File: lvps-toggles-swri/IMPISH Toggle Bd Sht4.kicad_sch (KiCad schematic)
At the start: 66 parts, among them J5 BCS-110-L-D-TE, J6 BCS-110-L-D-TE, Q13 MMBT3904Q, Q14 MMBT3906Q, Q15 ZXM61N02F, Q16 MMBT3904Q, Q17 MMBT3906Q, Q18 ZXM61N02F, Q19 MMBT3904Q, Q20 MMBT3906Q, Q21 ZXM61N02F, Q22 MMBT3904Q, Q23 MMBT3906Q, Q24 ZXM61N02F, U10 BSP452, U11 AP22804AW5-7, U12 AP22804AW5-7, U7 BSP452, U8 AP22804AW5-7, U9 AP22804AW5-7

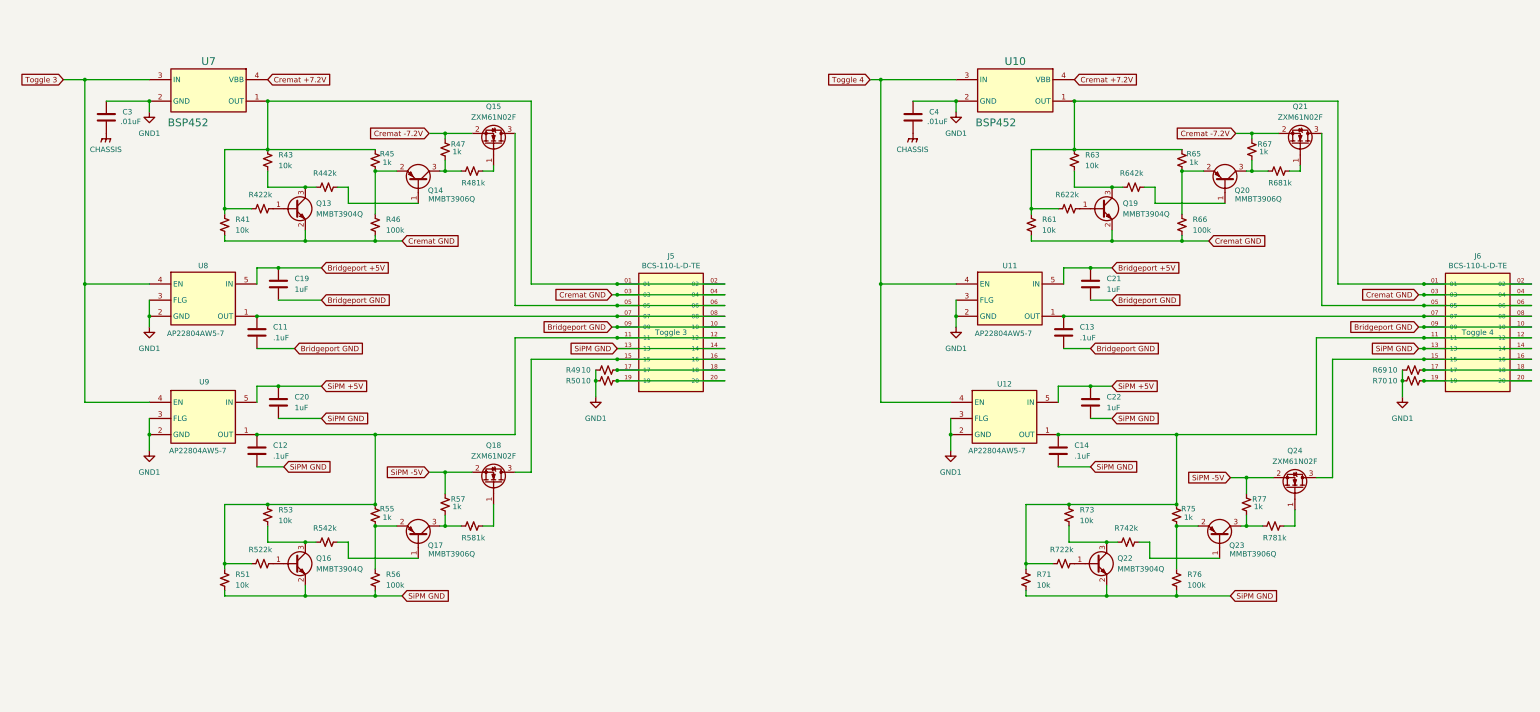
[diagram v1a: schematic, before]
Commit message: swri toggles: start one ground
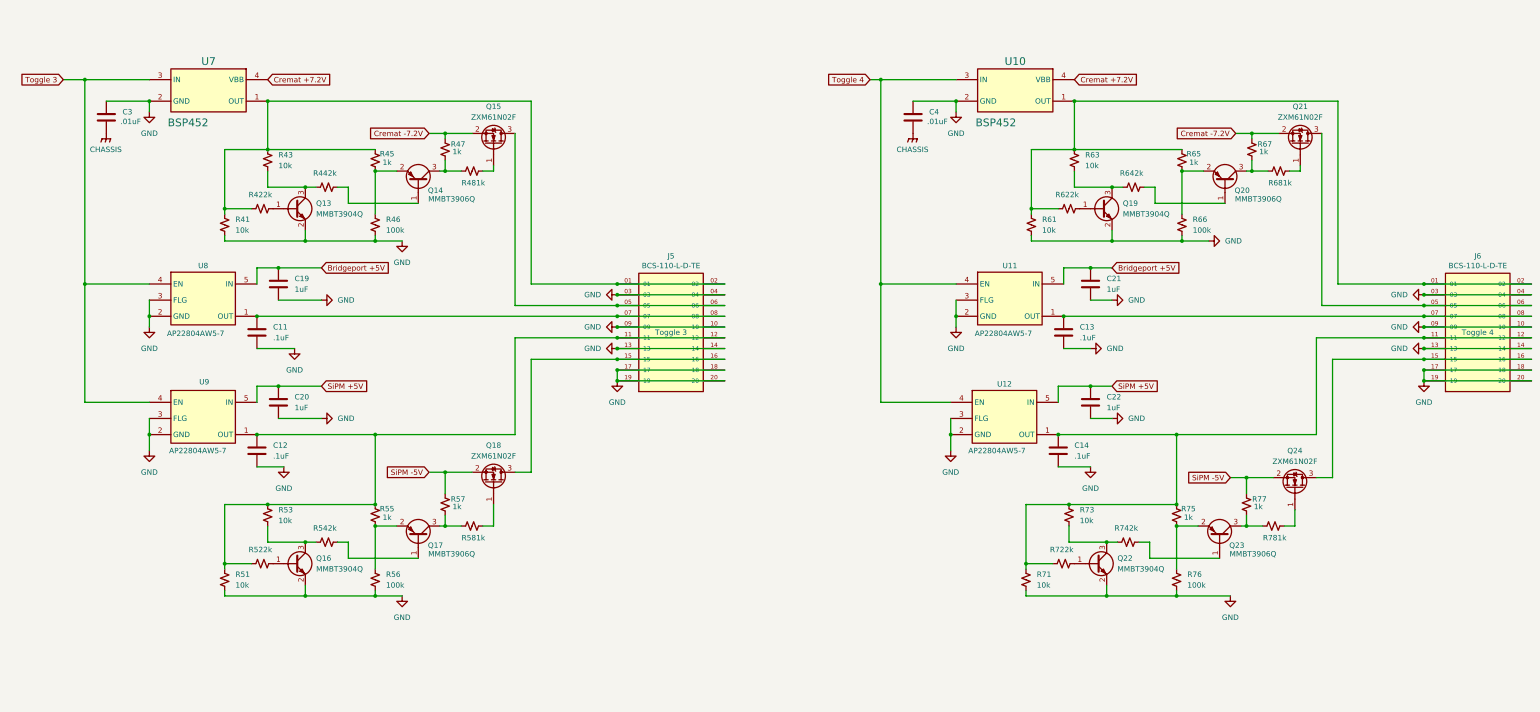
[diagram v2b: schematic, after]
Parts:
- removed R49, R50, R69, R70: 10, Resistor_SMD:R_0805_2012Metric_Pad1.20x1.40mm_HandSolder, symbol Device:R_Small_US
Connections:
- net Bridgeport GND is gone; now on net GND: C11.2, C13.2, C19.2, C21.2, J5.09, J5.10, J6.09, J6.10
- net Cremat GND is gone; now on net GND: J5.03, J5.04, J6.03, J6.04, Q13.2 (E), Q19.2 (E), R41.2, R46.2, R61.2, R66.2
- net GND1 is gone; now on net GND: C3.2, C4.2, U10.2 (GND), U11.2 (GND), U11.3 (FLG), U12.2 (GND), U12.3 (FLG), U7.2 (GND), U8.2 (GND), U8.3 (FLG), U9.2 (GND), U9.3 (FLG)
- net SiPM GND is gone; now on net GND: C12.2, C14.2, C20.2, C22.2, J5.13, J5.14, J6.13, J6.14, Q16.2 (E), Q22.2 (E), R51.2, R56.2, R71.2, R76.2
- net GND: now reaches J5.17, J5.18
- net GND: now also J5.19, J5.20, J6.17, J6.18, J6.19, J6.20

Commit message: toggles
remove cremat, fix layout, add DAQBOX toggle/power line
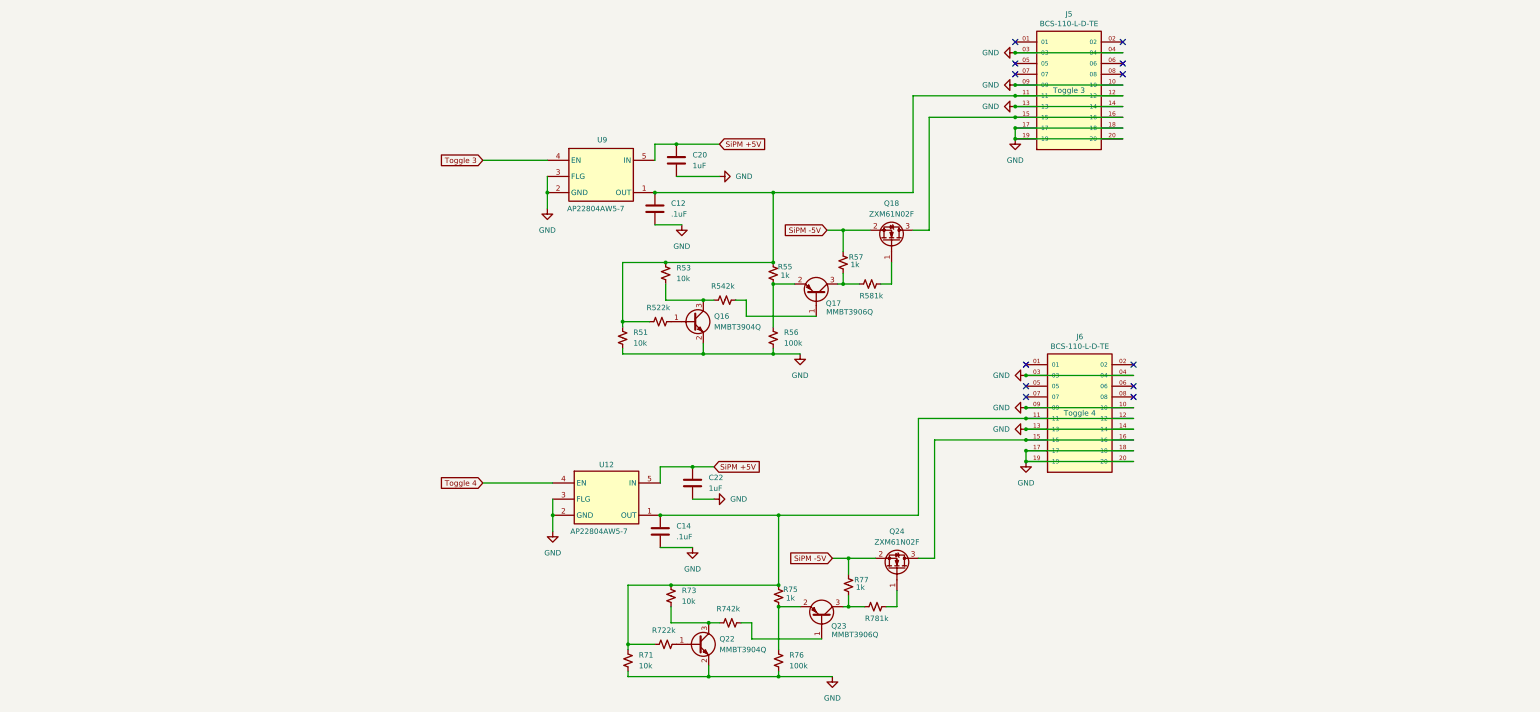
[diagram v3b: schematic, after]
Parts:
- removed C11, C13: .1uF, Capacitor_SMD:C_0805_2012Metric_Pad1.18x1.45mm_HandSolder, symbol IMPISH Toggles Library:.1uF
- removed C19, C21: 1uF, Capacitor_SMD:C_0805_2012Metric_Pad1.18x1.45mm_HandSolder, symbol IMPISH Toggles Library:1uF
- removed C3, C4: .01uF, Capacitor_SMD:C_0805_2012Metric_Pad1.18x1.45mm_HandSolder, symbol IMPISH Toggles Library:.01uF
- removed Q13, Q19: MMBT3904Q, Package_TO_SOT_SMD:SOT-23, symbol Transistor_BJT:MMBT3904
- removed Q14, Q20: MMBT3906Q, Package_TO_SOT_SMD:SOT-23, symbol Transistor_BJT:MMBT3906
- removed Q15, Q21: ZXM61N02F, Package_TO_SOT_SMD:SOT-23, symbol IMPISH Toggles Library:ZXM61N02F
- removed R41, R43, R61, R63: 10k, Resistor_SMD:R_0805_2012Metric_Pad1.20x1.40mm_HandSolder, symbol Device:R_Small_US
- removed R42, R44, R62, R64: 2k, Resistor_SMD:R_0805_2012Metric_Pad1.20x1.40mm_HandSolder, symbol Device:R_Small_US
- removed R45, R47, R48, R65, R67, R68: 1k, Resistor_SMD:R_0805_2012Metric_Pad1.20x1.40mm_HandSolder, symbol Device:R_Small_US
- removed R46, R66: 100k, Resistor_SMD:R_0805_2012Metric_Pad1.20x1.40mm_HandSolder, symbol Device:R_Small_US
- removed U10, U7: BSP452, IMPISH Toggles Library:SOT230P700X180-4N-3-V, symbol IMPISH Toggles Library:BSP452
- removed U11, U8: AP22804AW5-7, IMPISH Toggles Library:SOT95P285X140-5N, symbol IMPISH Toggles Library:AP22804AW5-7
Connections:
- net at J5.07: no longer J5.08
- net at J5.05: no longer J5.06
- net at J5.01: no longer J5.02
- net at J6.01: no longer J6.02
- net at J6.07: no longer J6.08
- net at J6.05: no longer J6.06
- no-connect marks 0 -> 12
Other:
- moved on the sheet: C12, C14, C20, C22, J5, J6, Q16, Q17, Q18, Q22, Q23, Q24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
